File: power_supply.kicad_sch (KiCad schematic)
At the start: 62 parts, among them Q10 AO3401A, Q13 AO3400A, Q14 AO3400A, Q3 AO3400A, Q5 AO3400A, Q8 AO3401A, SW2 SW_DPDT_x2, U2 AP9101CK6, U6 BQ21040DBV, U7 74HC14

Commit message: more readable schematic, bipolar supply
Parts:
- removed U2: AP9101CK6, Package_TO_SOT_SMD:SOT-23-6, symbol Battery_Management:AP9101CK6
- added U8: AP9101CK6, Package_TO_SOT_SMD:SOT-23-6_Handsoldering, symbol PEKG_lib:AP9101CK6
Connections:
- net -BATT: now also U8.6 (VSS)
- net Earth: no longer C1.1, C111.1, C17.1, C3.1, C31.1, C40.1, C46.1, C5.1, C51.1, C52.1, C53.1, C54.1, C59.1, C63.1, C64.1, C7.1, D13.1 (K), D8.1 (K), Q10.2 (S), Q13.2 (S), Q5.2 (S), R25.2, R6.1, R8.1, U6.5 (GND), U7.7 (GND)
- net at C6.2, R30.2: now also U8.5 (VDD)
- net at R8.2: now also U8.2 (VM)
- net at Q3.1 (G): now also U8.1 (DO)
- net at Q5.1 (G): now also U8.3 (CO)
- new net GND: C1.1, C111.1, C17.1, C3.1, C31.1, C40.1, C46.1, C5.1, C51.1, C52.1, C53.1, C54.1, C59.1, C63.1, C64.1, C7.1, D13.1 (K), D8.1 (K), Q10.2 (S), Q13.2 (S), Q5.2 (S), R25.2, R6.1, R8.1, U6.5 (GND), U7.7 (GND)
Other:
- moved on the sheet: BT2, C6, Q3, Q5, R30, R8

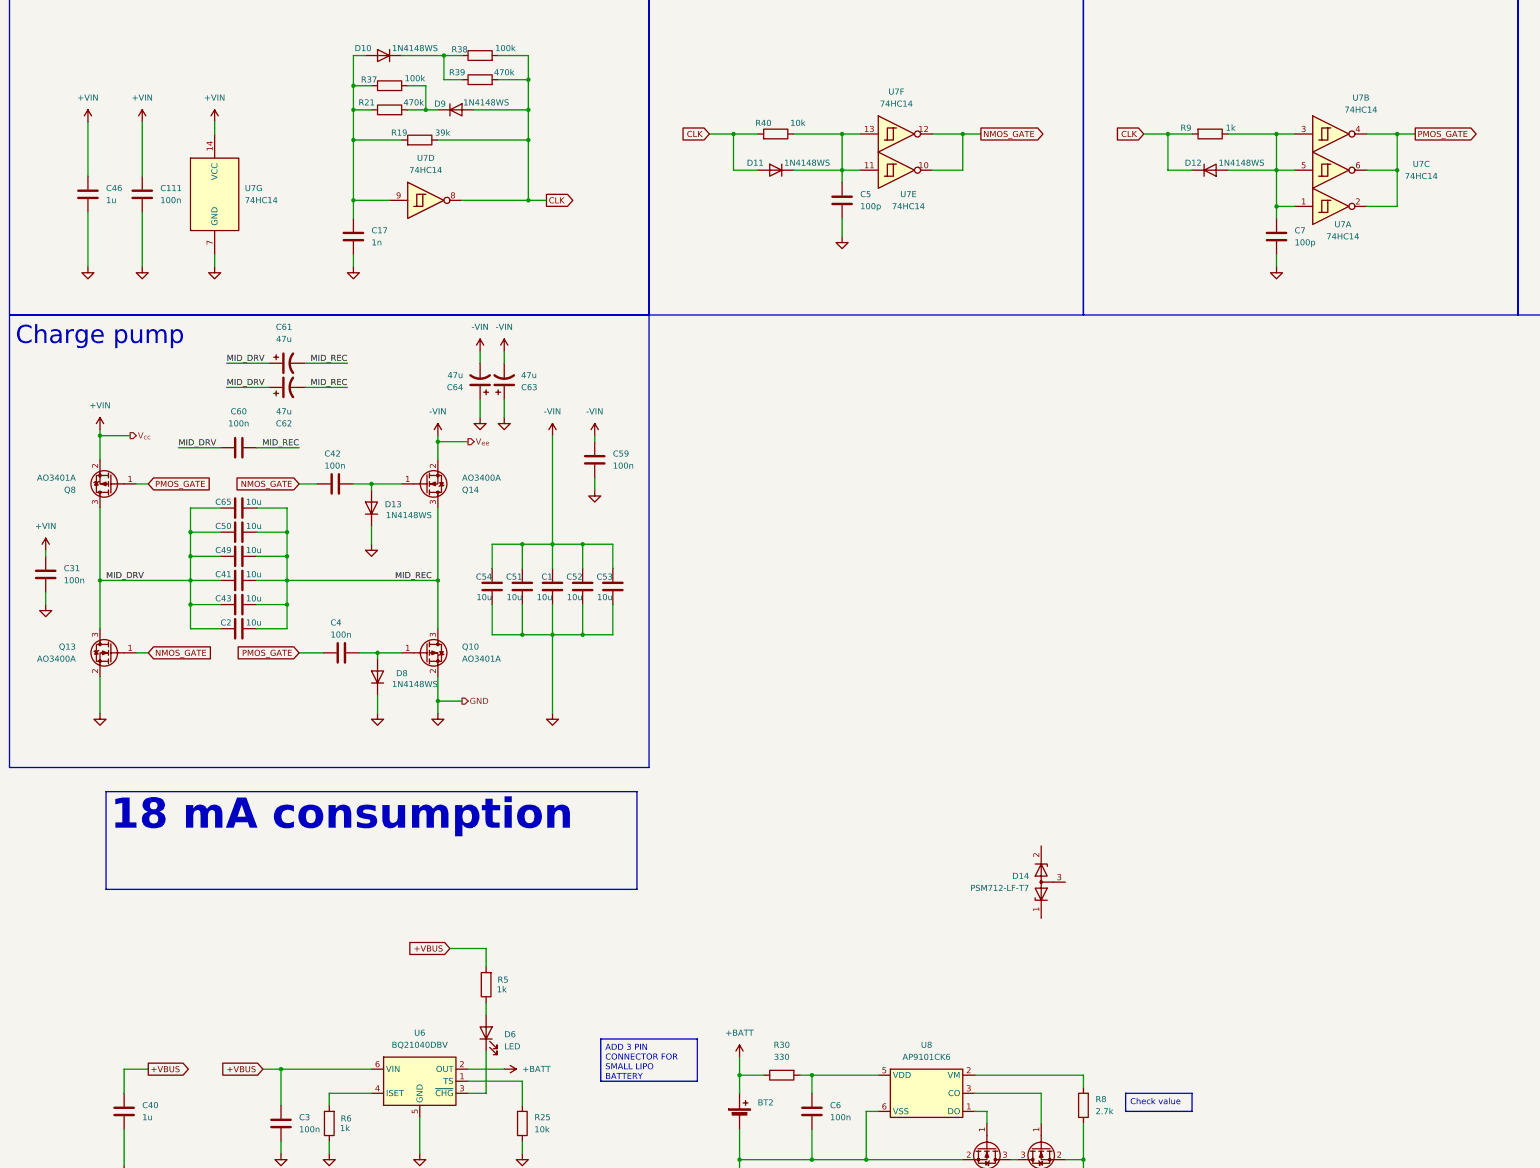
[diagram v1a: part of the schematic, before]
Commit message: Added ESP32-S3
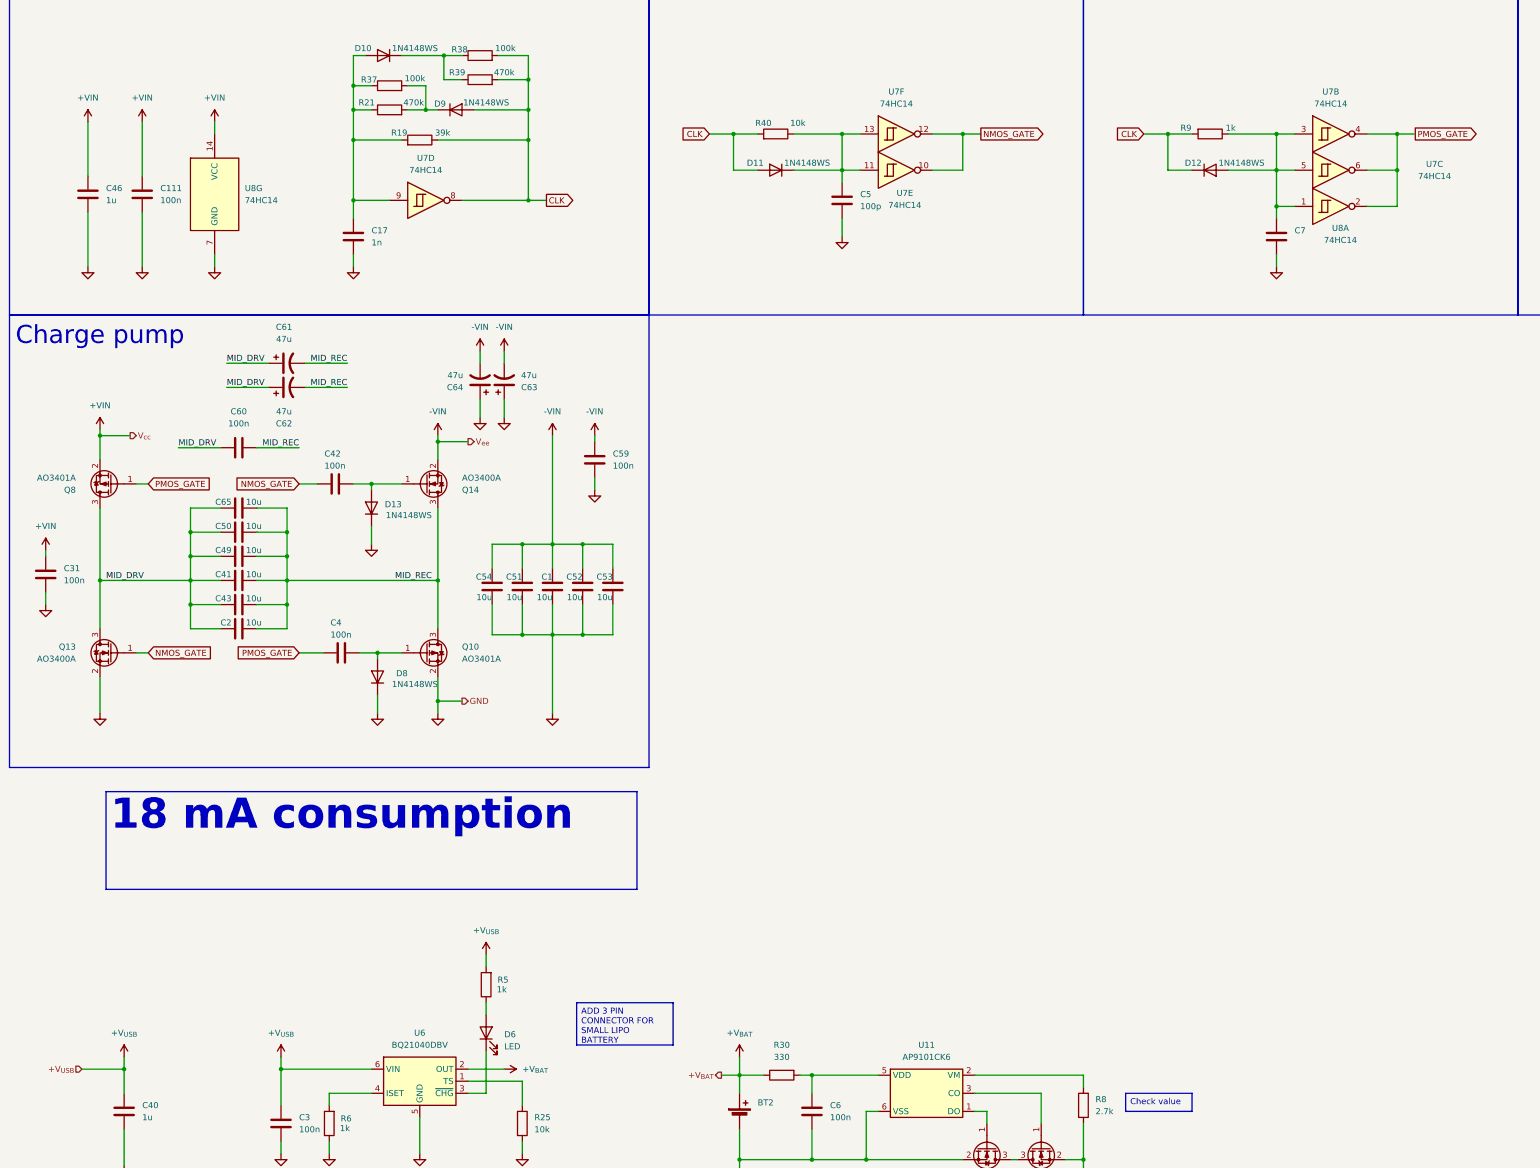
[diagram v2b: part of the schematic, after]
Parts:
- removed D14: PSM712-LF-T7, Package_TO_SOT_SMD:SOT-23_Handsoldering, symbol Device:D_Zener_Dual_CommonAnode_KKA
- removed unit 1 of U7
- removed unit 7 of U7
- added U8: 74HC14, symbol 74xx:74HC14
- U7: footprint Package_SO:SOIC-14_3.9x8.7mm_P1.27mm -> (none)
- renumbered U8 to U11
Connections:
- net +BATT: no longer BT2.1 (+), R30.1, U6.2 (OUT)
- net +VIN: now also U8.14 (VCC)
- net GND: now also U8.7 (GND)
- net PMOS_GATE: now also U8.2
- net at C7.2, D12.2 (A), R9.1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: now also U8.1
- net +VBUS renamed +V_{USB}
- new net +V_{BAT}: BT2.1 (+), R30.1, U6.2 (OUT)
